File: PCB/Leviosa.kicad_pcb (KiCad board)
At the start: 2 copper layers, 80 x 80 mm, 59 parts, among them J1 Barrel_Jack, J2 2.54mm 1x03 Spare, Q1 NCE0110K, U1 TPS1H200AQDGNRQ1, U2 MC7805BD2TR4G, U3 SS495A, U4 MCP6001R, U5 LM393, U6 MX27517, U7 INA199xxDCK (50V/V)

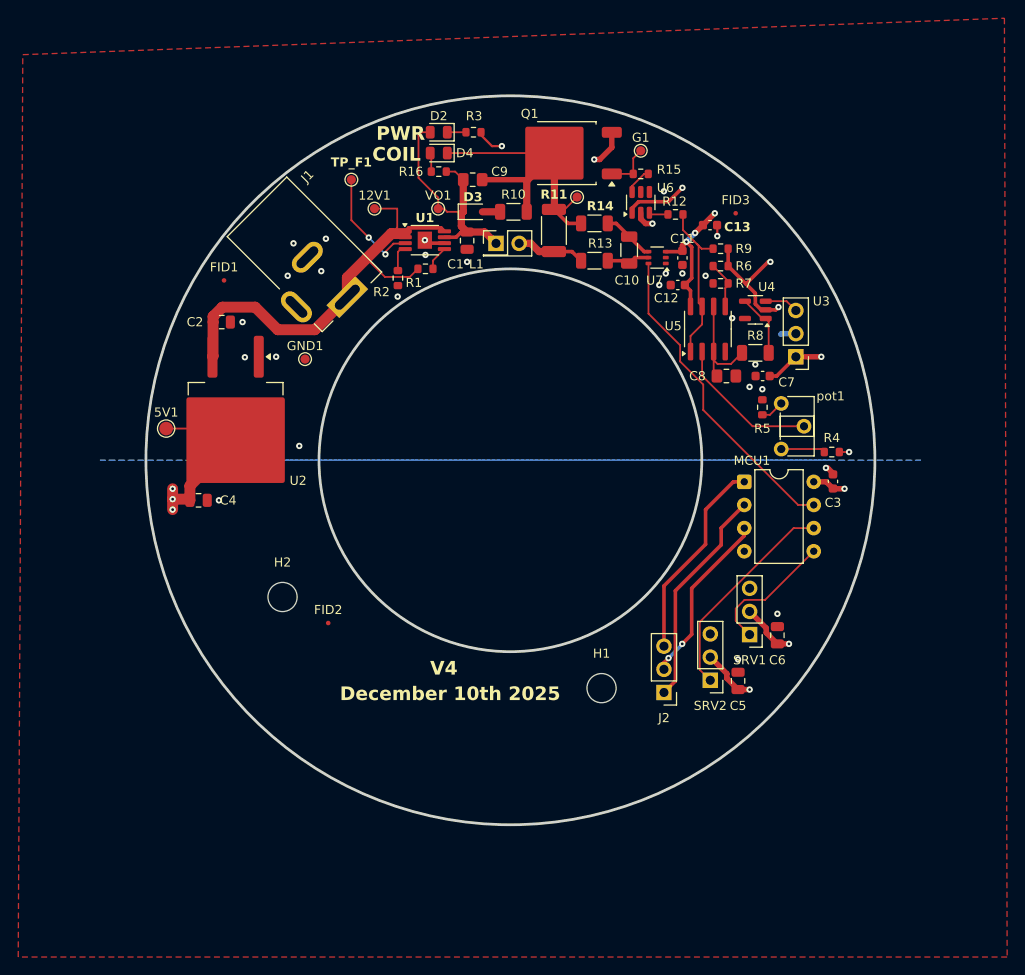
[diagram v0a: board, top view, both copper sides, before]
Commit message: cleanup and erc fixes. ready for pcb design
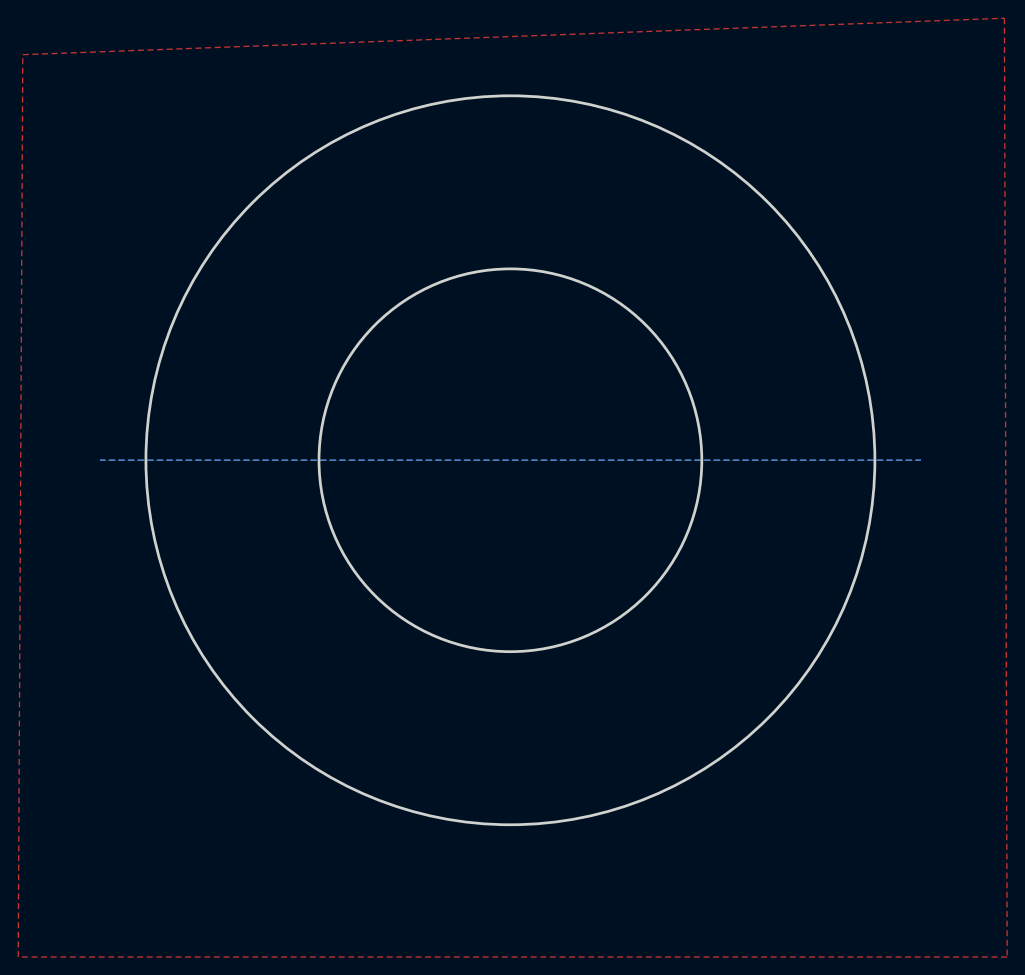
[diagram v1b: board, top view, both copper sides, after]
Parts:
- removed 12V1: 12V, TestPoint:TestPoint_Pad_D1.0mm
- removed 5V1: 5V, TestPoint:TestPoint_Pad_D1.5mm
- removed C1, C5, C6: 22µF, Capacitor_SMD:C_0805_2012Metric
- removed C10: 47μF, Capacitor_SMD:C_1206_3216Metric
- removed C11, C3: 0.1µF, Capacitor_SMD:C_0603_1608Metric
- removed C12, C13, C7: 0.1uF, Capacitor_SMD:C_0603_1608Metric
- removed C2, C4: 0.33µF, Capacitor_SMD:C_0805_2012Metric
- removed C8: 4.7nF, Capacitor_SMD:C_0805_2012Metric_Pad1.18x1.45mm_HandSolder
- removed C9: 20nF, Capacitor_SMD:C_0805_2012Metric_Pad1.18x1.45mm_HandSolder
- removed D2, D4: LED, LED_SMD:LED_0805_2012Metric
- removed D3: SS34, Diode_SMD:D_SOD-323
- removed FID1, FID2, FID3: Fiducial, Fiducial:Fiducial_0.5mm_Mask1mm
- removed G1: set_point_trigger, TestPoint:TestPoint_Pad_D1.0mm
- removed GND1: GND, TestPoint:TestPoint_Pad_D1.0mm
- removed H1, H2: MountingHole, MountingHole:MountingHole_3.2mm_M3_ISO7380
- removed J1: Barrel_Jack, Connector_BarrelJack:BarrelJack_Kycon_KLDX-0202-xC_Horizontal
- removed J2: 2.54mm 1x03 Spare, Connector_PinHeader_2.54mm:PinHeader_1x03_P2.54mm_Vertical
- removed L1: 7.4mH, Connector_PinHeader_2.54mm:PinHeader_2x01_P2.54mm_Vertical
- removed MCU1: ATtiny13A-P, Package_DIP:DIP-8_W7.62mm
- removed Q1: NCE0110K, Package_TO_SOT_SMD:TO-252-2
- removed R1, R6: 100kΩ, Resistor_SMD:R_0603_1608Metric
- removed R10, R13, R14, R8: 8.2Ω, Resistor_SMD:R_1206_3216Metric
- removed R11: 50mΩ, Resistor_SMD:R_2010_5025Metric
- removed R12, R15: 0Ω, Resistor_SMD:R_0603_1608Metric
- removed R16, R3: 2kΩ, Resistor_SMD:R_0603_1608Metric
- removed R2, R5, R9: 3.9kΩ, Resistor_SMD:R_0603_1608Metric
- removed R4: 51kΩ, Resistor_SMD:R_0603_1608Metric
- removed R7: 68kΩ, Resistor_SMD:R_0603_1608Metric
- removed SRV1, SRV2: 2.54mm 1x03 Servo 1, Connector_PinHeader_2.54mm:PinHeader_1x03_P2.54mm_Vertical
- removed TP_COIL1: Coil Output, TestPoint:TestPoint_Pad_D1.0mm
- removed TP_F1: Fault, TestPoint:TestPoint_Pad_D1.0mm
- removed U1: TPS1H200AQDGNRQ1, Package_SO:HVSSOP-8-1EP_3x3mm_P0.65mm_EP1.57x1.89mm
- removed U2: MC7805BD2TR4G, Package_TO_SOT_SMD:TO-263-2
- removed U3: SS495A, Connector_PinHeader_2.54mm:PinHeader_1x03_P2.54mm_Vertical
- removed U4: MCP6001R, Package_TO_SOT_SMD:SOT-23-5
- removed U5: LM393, Package_SO:SOIC-8_3.9x4.9mm_P1.27mm
- removed U6: MX27517, Package_TO_SOT_SMD:SOT-23-6
- removed U7: INA199xxDCK (50V/V), Package_TO_SOT_SMD:SOT-363_SC-70-6
- removed VO1: Vout, TestPoint:TestPoint_Pad_D1.0mm
- removed pot1: 3362S-1-103LF, Potentiometer_THT:Potentiometer_ACP_CA6-H2,5_Horizontal
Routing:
- net +5V: track 86.7 -> 0.00 mm, vias 14 -> 0
- net +12V: track 49.6 -> 0.00 mm
- net /COIL_OUT: track 41.5 -> 0.00 mm
- net /CURT_SN: track 35.0 -> 0.00 mm
- net +12V_SF: track 28.0 -> 0.00 mm
- net /PB3: track 24.2 -> 0.00 mm
- net /SVR1_CTRL: track 23.6 -> 0.00 mm
- net /PB5: track 22.4 -> 0.00 mm
- net /PB4: track 19.1 -> 0.00 mm, vias 2 -> 0
- net /COMP_OUT: track 18.3 -> 0.00 mm
- net /SET_PT: track 16.1 -> 0.00 mm
- net GND: track 15.7 -> 0.00 mm, vias 29 -> 0
- net /SVR2_CTRL: track 14.6 -> 0.00 mm
- net Net-(U5A-+): track 12.5 -> 0.00 mm
- net Net-(U1-~{FAULT}): track 12.0 -> 0.00 mm, vias 2 -> 0
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- removed copper zone on B.Cu, net GND
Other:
- board text removed: "COIL"
- board text removed: "December 10th 2025"
- board text removed: "PWR"
- board text removed: "V4"
